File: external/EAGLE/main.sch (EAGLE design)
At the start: 6 parts, among them IC1 AD590ZR, IC2 L293D, J1 1-794681-6, X2 332-02

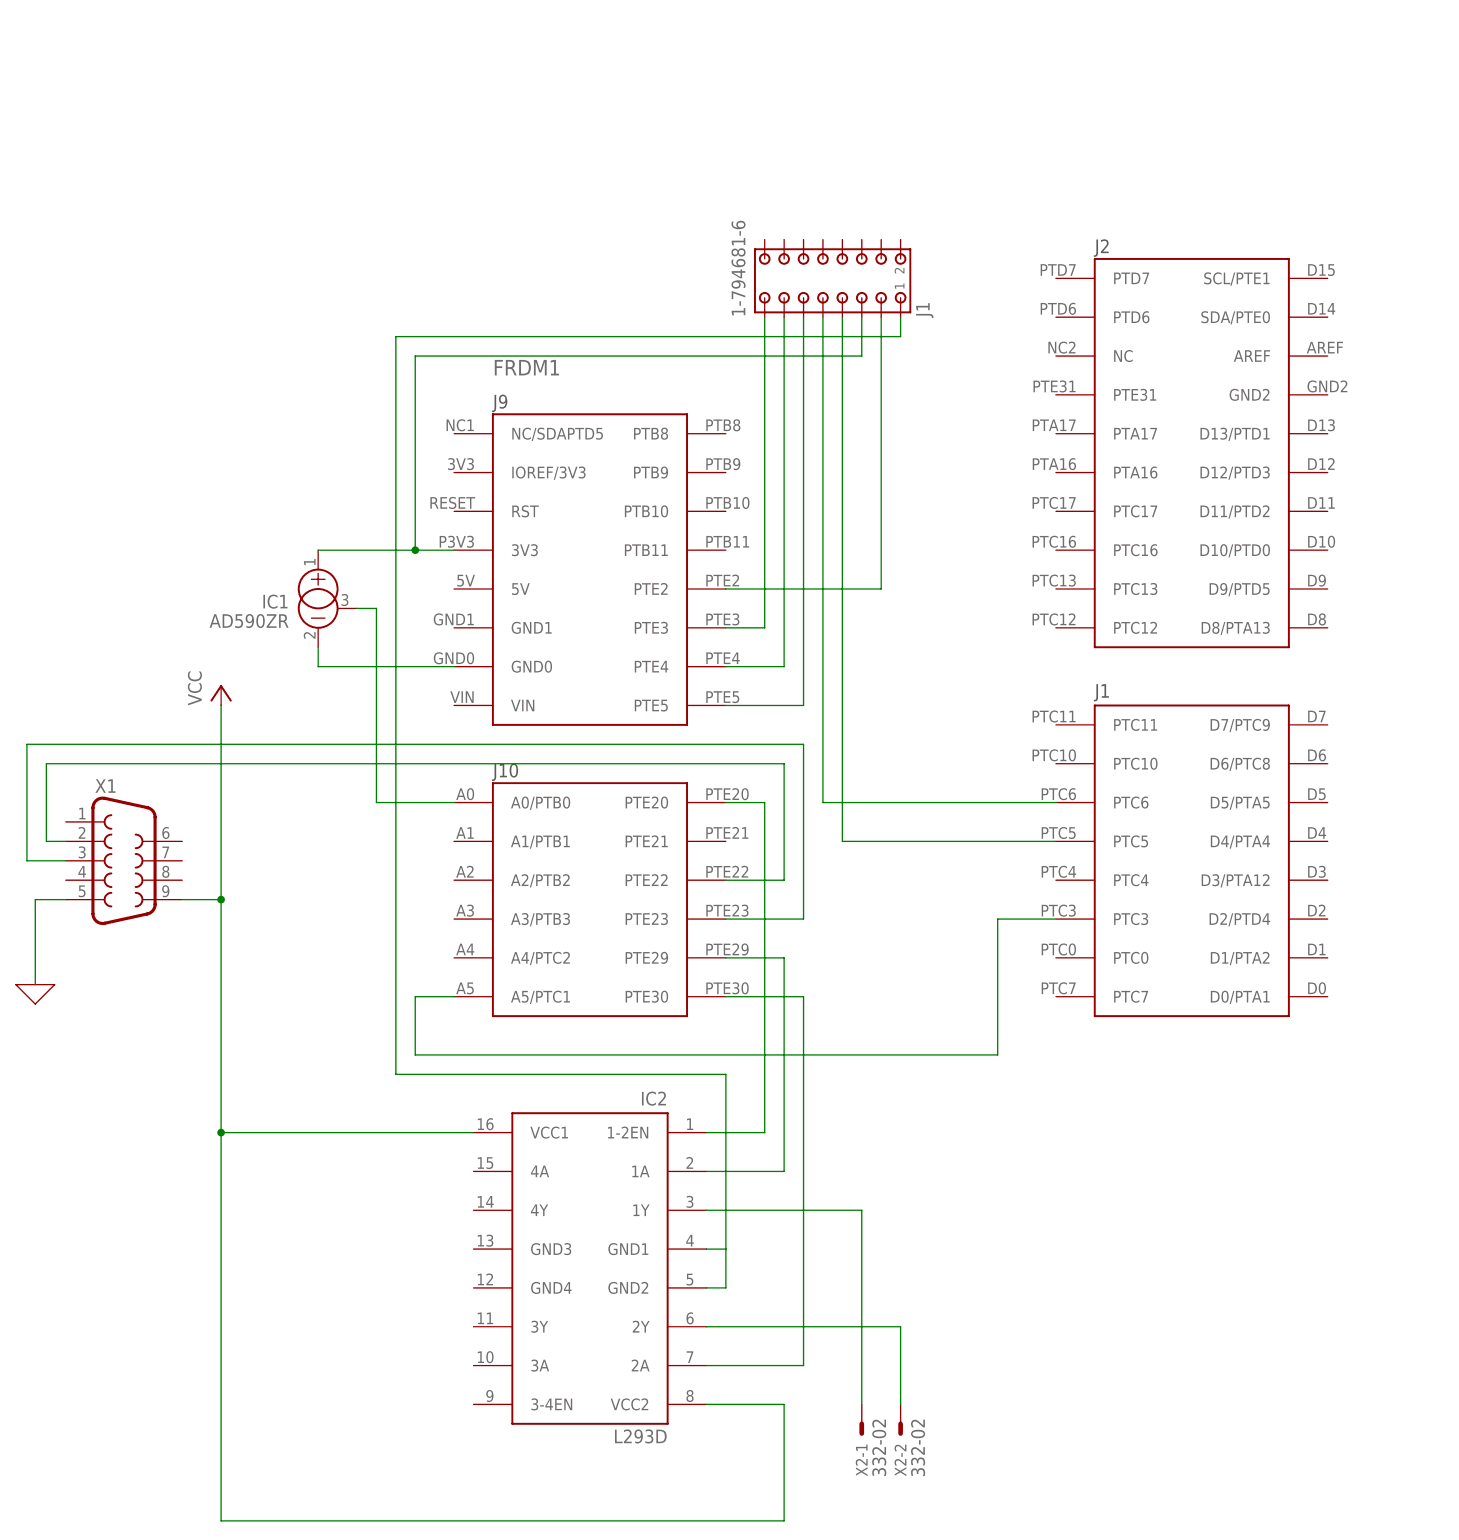
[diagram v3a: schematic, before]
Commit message: Updating schematic with EEPROM memory
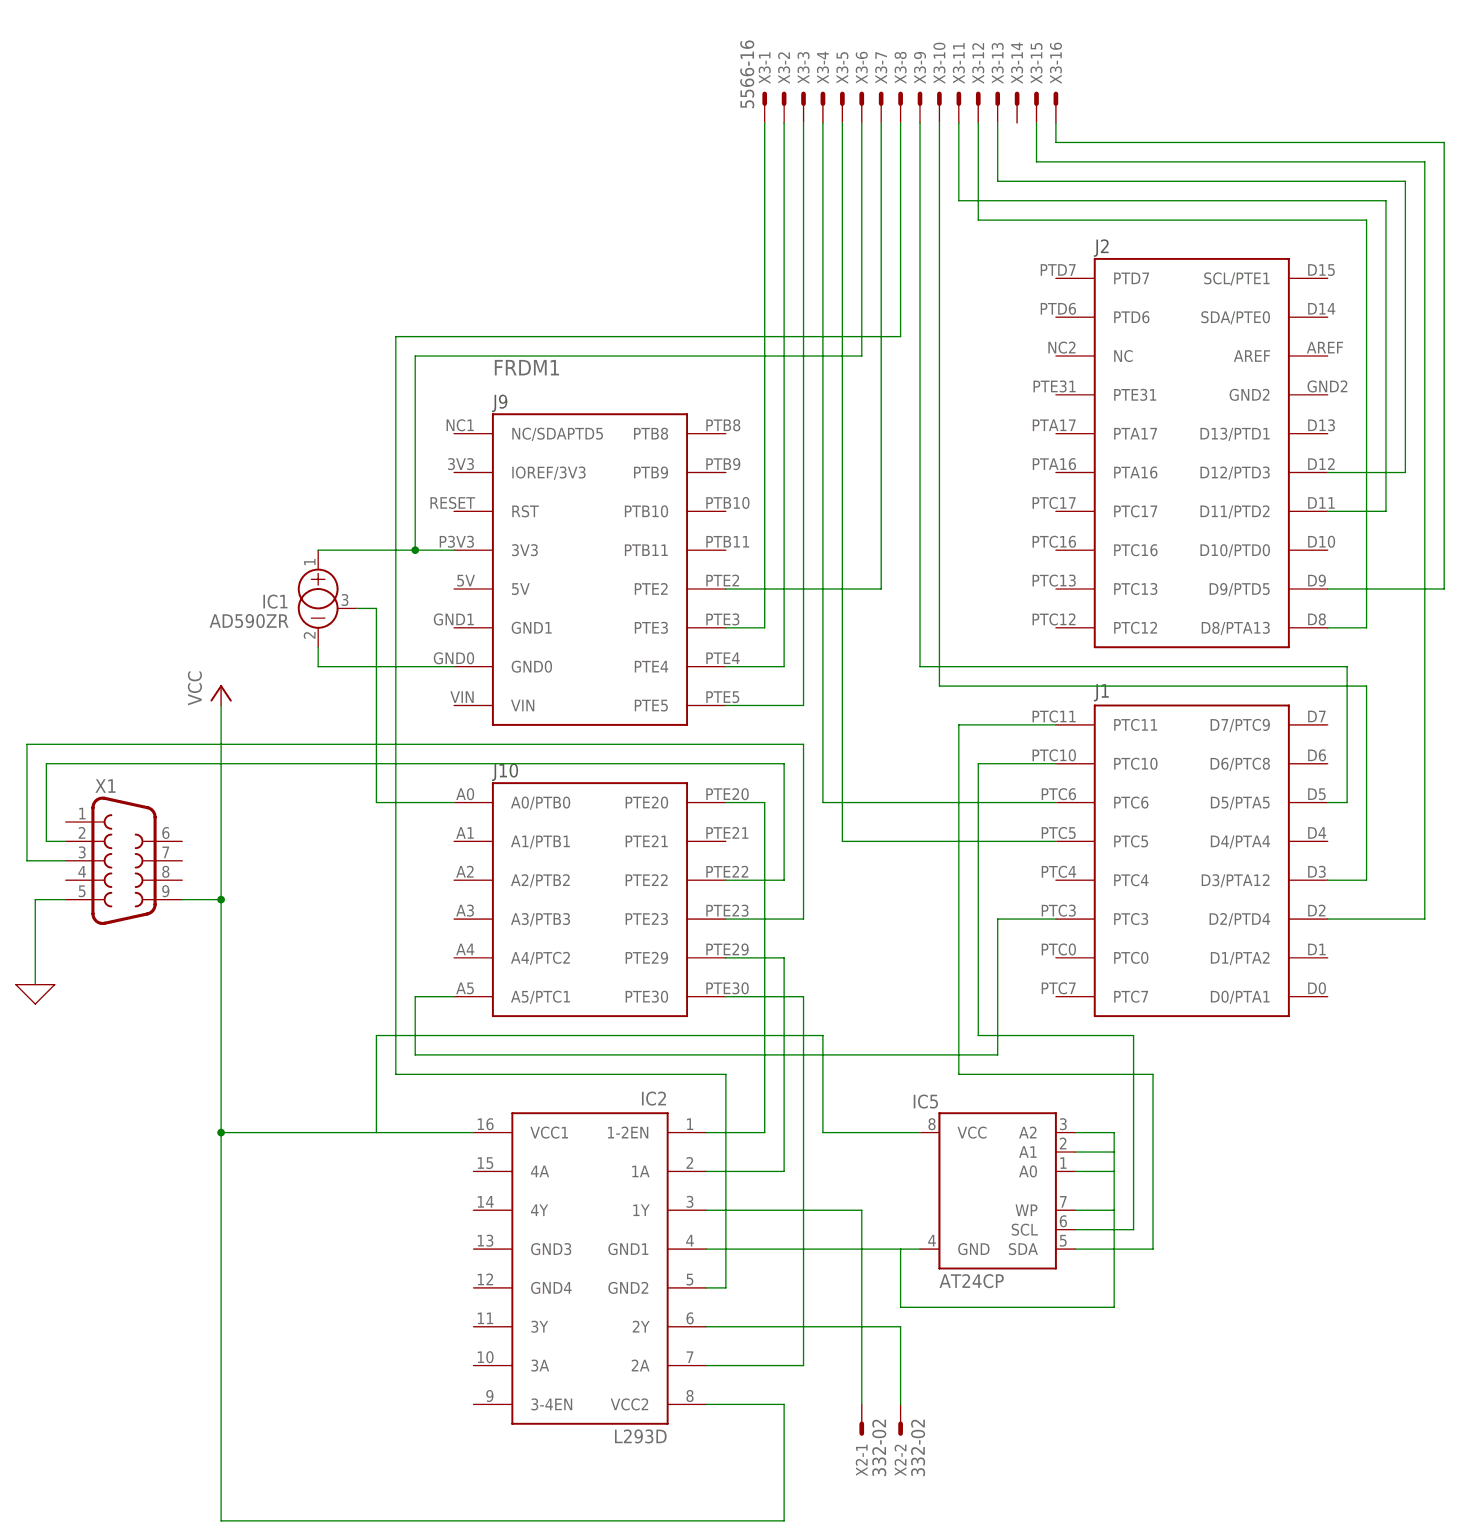
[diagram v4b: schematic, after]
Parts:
- removed J1: 1-794681-6, con-amp:1-794681-6
- added IC5: AT24CP, atmel:AT24CP
- added X3: 5566-16, con-molex:5566-16
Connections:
- new net N$18: FRDM1.D5/PTA5, X3-9.S
- new net N$19: FRDM1.D3/PTA12, X3-10.S
- new net N$20: FRDM1.D8/PTA13, X3-12.S
- new net N$21: FRDM1.D11/PTD2, X3-11.S
- new net N$22: FRDM1.D12/PTD3, X3-13.S
- new net N$23: FRDM1.D2/PTD4, X3-15.S
- new net N$24: FRDM1.D9/PTD5, X3-16.S
- new net N$27: FRDM1.PTC10, IC5.SCL
- new net N$28: FRDM1.PTC11, IC5.SDA
- net N$11: now also IC5.A0, IC5.A1, IC5.A2, IC5.GND, IC5.WP, X3-8.S; no longer J1.1
- net N$12: now also X3-1.S; no longer J1.15
- net N$13: now also X3-3.S; no longer J1.11
- net N$14: now also X3-2.S; no longer J1.13
- net N$15: now also X3-7.S; no longer J1.3
- net N$16: now also X3-4.S; no longer J1.9
- net N$17: now also X3-5.S; no longer J1.7
- net N$6: now also X3-6.S; no longer J1.5
- net VCC: now also IC5.VCC

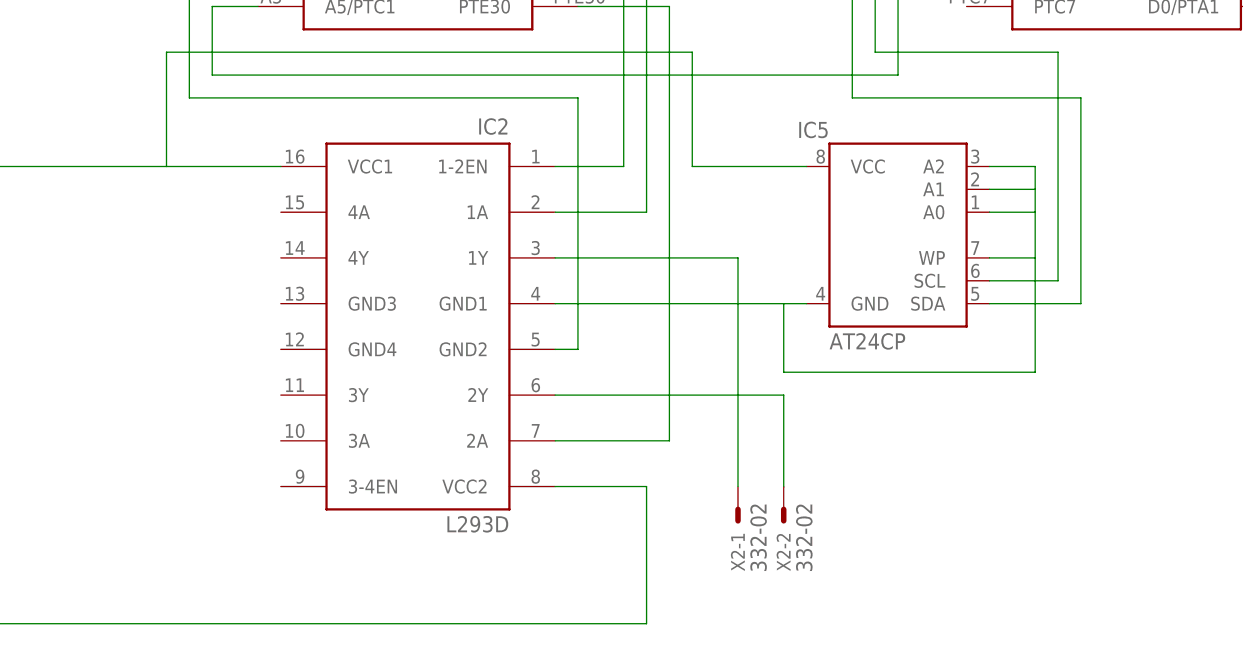
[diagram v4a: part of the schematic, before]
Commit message: Updating the schematic with pull-ups in SDA and SCL pins of EEPROM memory
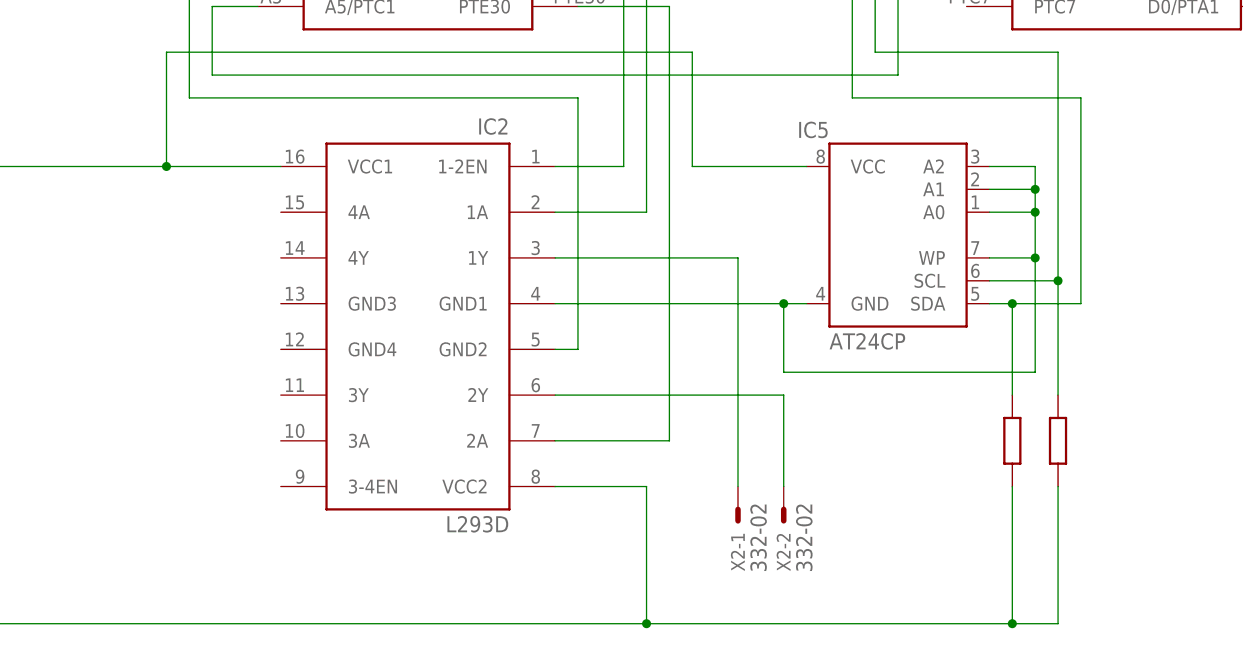
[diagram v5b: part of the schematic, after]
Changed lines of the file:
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@@
 <part name="X3" library="con-molex" library_urn="urn:adsk.eagle:library:165" deviceset="5566-16" device=""/>
 <part name="IC5" library="atmel" library_urn="urn:adsk.eagle:library:105" deviceset="AT24C*" device="P" package3d_urn="urn:adsk.eagle:package:4324/1"/>
+<part name="R1" library="docu-dummy" library_urn="urn:adsk.eagle:library:215" deviceset="R" device=""/>
+<part name="R2" library="docu-dummy" library_urn="urn:adsk.eagle:library:215" deviceset="R" device=""/>
 </parts>
 <sheets>
@@
 <attribute name="VALUE" x="129.54" y="-99.06" size="1.778" layer="96"/>
 </instance>
+<instance part="R1" gate="G$1" x="149.86" y="-109.22" smashed="yes" rot="R90"/>
+<instance part="R2" gate="G$1" x="154.94" y="-109.22" smashed="yes" rot="R90"/>
 </instances>
 <busses>
@@
 <wire x1="114.3" y1="-66.04" x2="55.88" y2="-66.04" width="0.1524" layer="91"/>
 <wire x1="55.88" y1="-66.04" x2="55.88" y2="-78.74" width="0.1524" layer="91"/>
+<wire x1="149.86" y1="-114.3" x2="149.86" y2="-129.54" width="0.1524" layer="91"/>
+<wire x1="149.86" y1="-129.54" x2="109.22" y2="-129.54" width="0.1524" layer="91"/>
+<wire x1="154.94" y1="-114.3" x2="154.94" y2="-129.54" width="0.1524" layer="91"/>
+<wire x1="154.94" y1="-129.54" x2="149.86" y2="-129.54" width="0.1524" layer="91"/>
+<junction x="109.22" y="-129.54"/>
+<junction x="55.88" y="-78.74"/>
+<junction x="149.86" y="-129.54"/>
 </segment>
 </net>
@@
 <pinref part="IC5" gate="G$1" pin="WP"/>
 <wire x1="147.32" y1="-88.9" x2="152.4" y2="-88.9" width="0.1524" layer="91"/>
+<junction x="124.46" y="-93.98"/>
+<junction x="152.4" y="-81.28"/>
+<junction x="152.4" y="-83.82"/>
+<junction x="152.4" y="-88.9"/>
 </segment>
 </net>
@@
 <pinref part="FRDM1" gate="G$1" pin="PTC10"/>
 <wire x1="134.62" y1="-30.48" x2="144.78" y2="-30.48" width="0.1524" layer="91"/>
+<wire x1="154.94" y1="-104.14" x2="154.94" y2="-91.44" width="0.1524" layer="91"/>
+<junction x="154.94" y="-91.44"/>
 </segment>
 </net>
@@
 <wire x1="157.48" y1="-71.12" x2="157.48" y2="-93.98" width="0.1524" layer="91"/>
 <pinref part="IC5" gate="G$1" pin="SDA"/>
-<wire x1="157.48" y1="-93.98" x2="147.32" y2="-93.98" width="0.1524" layer="91"/>
-</segment>
-</net>
+<wire x1="157.48" y1="-93.98" x2="149.86" y2="-93.98" width="0.1524" layer="91"/>
+<wire x1="149.86" y1="-93.98" x2="147.32" y2="-93.98" width="0.1524" layer="91"/>
+<wire x1="149.86" y1="-104.14" x2="149.86" y2="-93.98" width="0.1524" layer="91"/>
+<junction x="149.86" y="-93.98"/>
+</segment>
+</net>
